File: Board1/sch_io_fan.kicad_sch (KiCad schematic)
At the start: 9 parts, among them J8 Fan, Q2 DMN3010LK3, U5 VOS615A-1X001T

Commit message: v1.2 release of board with bug fixes etc
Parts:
- removed D2: 1N4148, Diode_SMD:Nexperia_CFP3_SOD-123W, symbol Device:D
- removed D3: SS15, Diode_SMD:D_SMA, symbol Diode:SS15
- removed Q2: DMN3010LK3, Package_TO_SOT_SMD:TO-252-2, symbol Transistor_FET:2N7002E
- removed R15: 4k7, Resistor_SMD:R_0603_1608Metric_Pad0.98x0.95mm_HandSolder, symbol Device:R_Small_US
- removed R7, R8: 220R, Resistor_SMD:R_0603_1608Metric_Pad0.98x0.95mm_HandSolder, symbol Device:R_Small_US
- removed R9: 10k, Resistor_SMD:R_0603_1608Metric_Pad0.98x0.95mm_HandSolder, symbol Device:R_Small_US
- removed U5: VOS615A-1X001T, Package_SO:SSOP-4_4.4x2.6mm_P1.27mm, symbol Isolator:PC817
- added C9: 0.1u, Capacitor_SMD:C_0603_1608Metric, symbol Device:C_Small
- added D4: SS12, Diode_SMD:D_SMA, symbol Diode:SS15
- added R12: 300, Resistor_SMD:R_0603_1608Metric, symbol Device:R
- added U3: DGD0280WT-7, Wattle_Mosfet_Drv:SOT23-5_INF, symbol Wattle_Mosfet_Drv:DGD0280WT-7
- added U5: DMN3010LK3-13, Wattle_Mosfets:TO252-3L_DIO, symbol Wattle_Mosfets:DMN3010LK3-13
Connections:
- net +5V: now also C9.1, D4.1 (K), U3.1 (Vcc)
- net FAN: now also U3.3 (IN)
- net GND: now also C9.2, U3.2 (COM), U5.3 (S)
- net at J8.1 (Pin_1): now also D4.2 (A), U5.2 (D)
- new net: R12.2, U3.5 (OUT)
- new net: R12.1, U5.1 (G)
- no-connect marks 0 -> 1
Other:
- moved on the sheet: J8

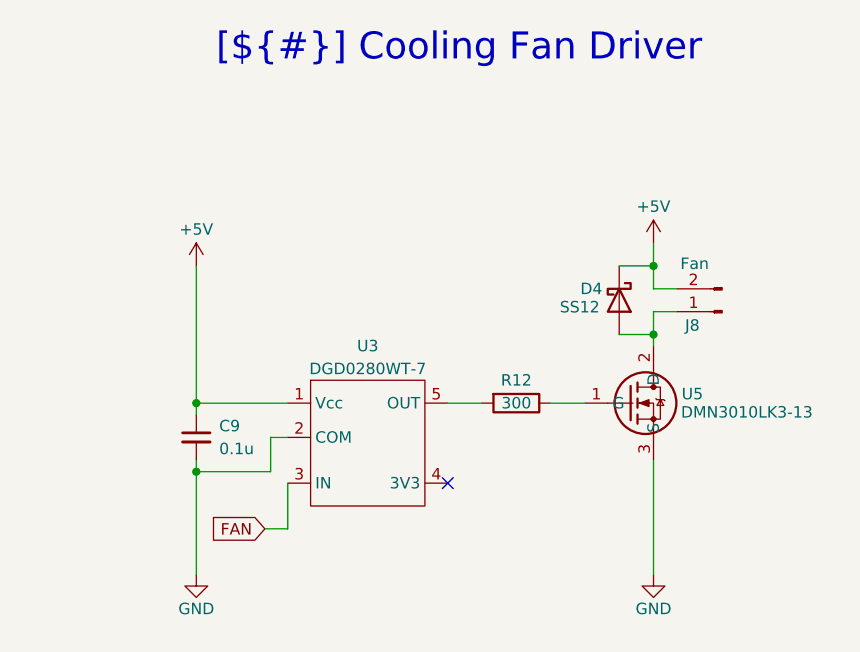
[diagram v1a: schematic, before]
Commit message: Tweaks to schematic for clarity and minor firmware
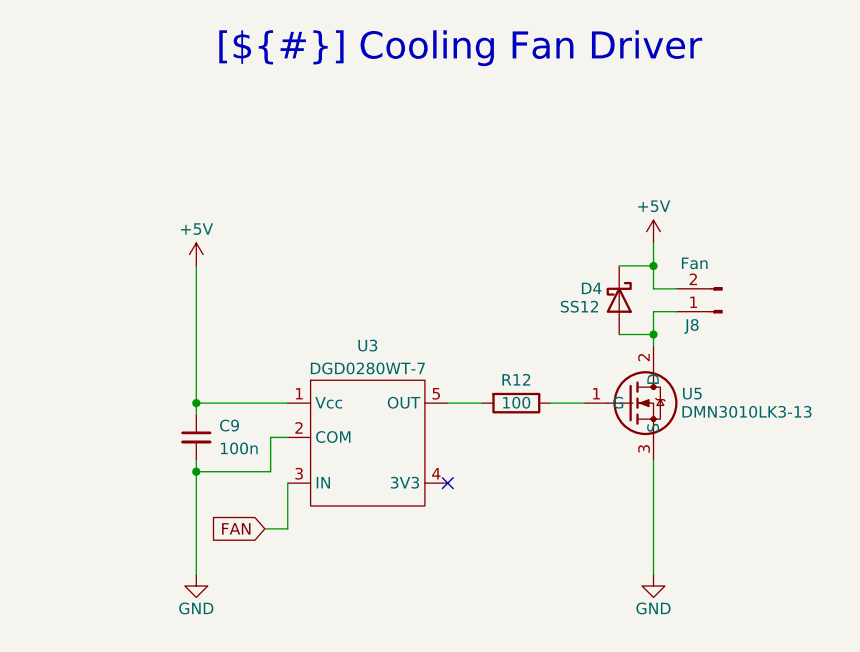
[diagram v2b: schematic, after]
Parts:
- C9: value 0.1u -> 100n; Digikey_PN (none) -> 399-C0603C104K4RACTUCT-ND
- R12: value 300 -> 100; Digikey_PN (none) -> 541-3951-1-ND
- U3: Digikey_PN (none) -> 31-DGD0280WT-7CT-ND
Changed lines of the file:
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@@
 	(title_block
 		(title "Cooling Fan Driver")
-		(date "2025-03-08")
+		(date "2025-03-10")
 		(rev "1.2")
 		(company "Wattle Labs")
@@
 			)
 		)
-		(property "Digikey_PN" ""
+		(property "Digikey_PN" "31-DGD0280WT-7CT-ND"
 			(at 138.43 64.77 0)
 			(effects
@@
 			)
 		)
-		(property "Value" "0.1u"
+		(property "Value" "100n"
 			(at 121.92 63.5 0)
 			(effects
@@
 			)
 		)
-		(property "Description" "0.1uF Ceramic 25V X5R"
+		(property "Description" "100nF Ceramic 16V X5R"
 			(at 119.38 62.23 0)
 			(effects
@@
 			)
 		)
-		(property "Digikey_PN" ""
+		(property "Digikey_PN" "399-C0603C104K4RACTUCT-ND"
 			(at 119.38 62.23 0)
 			(effects
@@
 			)
 		)
-		(property "Value" "300"
+		(property "Value" "100"
 			(at 154.94 58.42 90)
 			(effects
@@
 			)
 		)
-		(property "Description" "Resistor"
+		(property "Description" "RES 100 OHM 1% 1/10W 0603"
 			(at 154.94 58.42 0)
 			(effects
@@
 			)
 		)
-		(property "Digikey_PN" ""
+		(property "Digikey_PN" "541-3951-1-ND"
 			(at 154.94 58.42 0)
 			(effects
